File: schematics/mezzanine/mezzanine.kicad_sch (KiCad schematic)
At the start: 22 parts, among them J1 Bionic-P135, J10 Y0-7, J11 A0-7, J12 B0-7, J2 Bionic-P245, J3 Conn_01x24, J4 Conn_01x24, J5 P1P2, J6 P3P4, J7 P5, J8 5V0, J9 GND, U1 CPU, U2 11AA010-I/TT, U3 74AHCT157, U4 74AHCT157

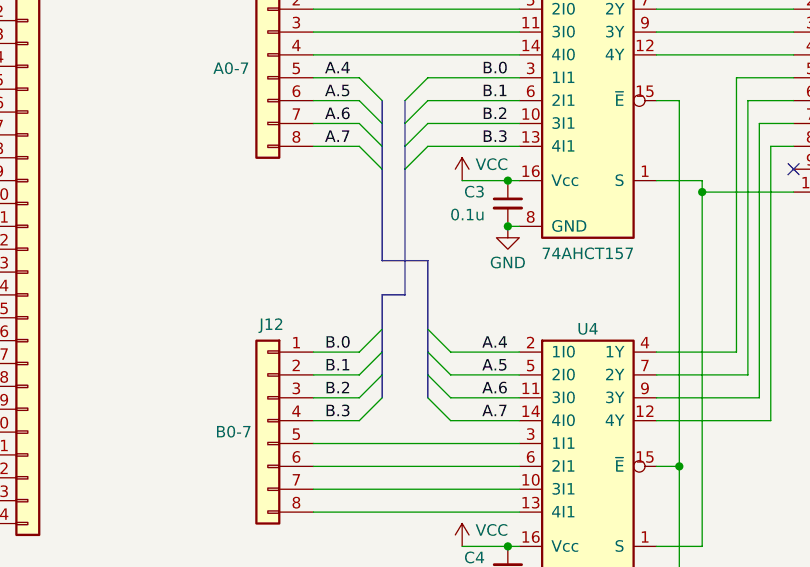
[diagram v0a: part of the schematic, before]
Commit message: [Mezzanine] Cleanup schematics
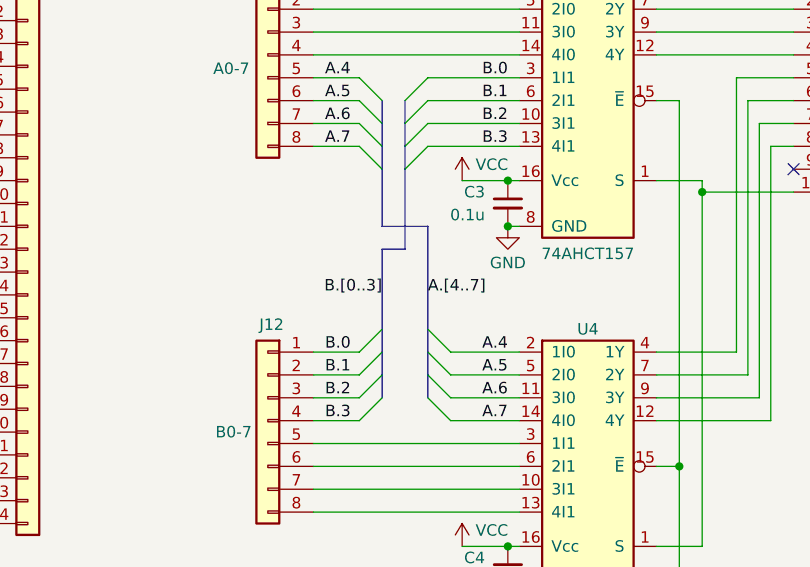
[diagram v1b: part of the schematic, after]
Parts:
- D1: footprint 0-LocalLibrary:LED_CSL1901UW1_ROM-M -> rhom:LED_CSL1901UW1_ROM-M; symbol 0-LocalLibrary:CSL1901UW1 -> rhom:CSL1901UW1
- J1: footprint 0-LocalLibrary:Bionic-P135_Vertical -> bionic:Bionic-P135_Vertical; symbol 0-LocalLibrary:Bionic-P135 -> bionic:Bionic-P135
- J2: footprint 0-LocalLibrary:Bionic-P245_Vertical -> bionic:Bionic-P245_Vertical; symbol 0-LocalLibrary:Bionic-P245 -> bionic:Bionic-P245
- U1: footprint 0-LocalLibrary:Aries_ZIF_socket_DIP-48-pin -> bionic:Aries_ZIF_socket_DIP-48-pin; symbol 0-LocalLibrary:CPU -> cpu:CPU
- U2: footprint 0-LocalLibrary:SOT-23_MC_MCH-M -> microchip:SOT-23_MC_MCH-M; symbol 0-LocalLibrary:11AA010-I_TT -> microchip:11AA010-I_TT
- U3, U4: footprint 0-LocalLibrary:PW16-M -> ti:PW16-M; symbol 0-LocalLibrary:74AHCT157 -> ti:74AHCT157

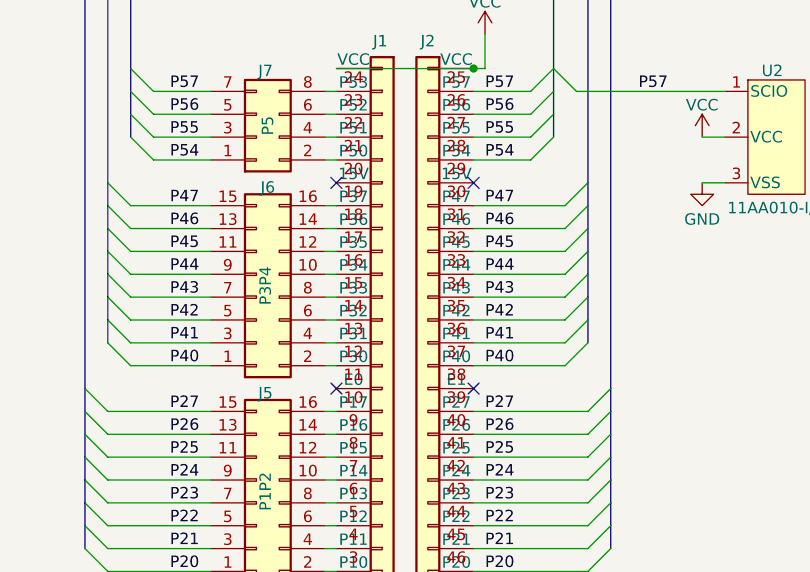
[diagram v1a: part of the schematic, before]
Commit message: [Mezzanine] Update schematics
Remove unused pins from bionic connector
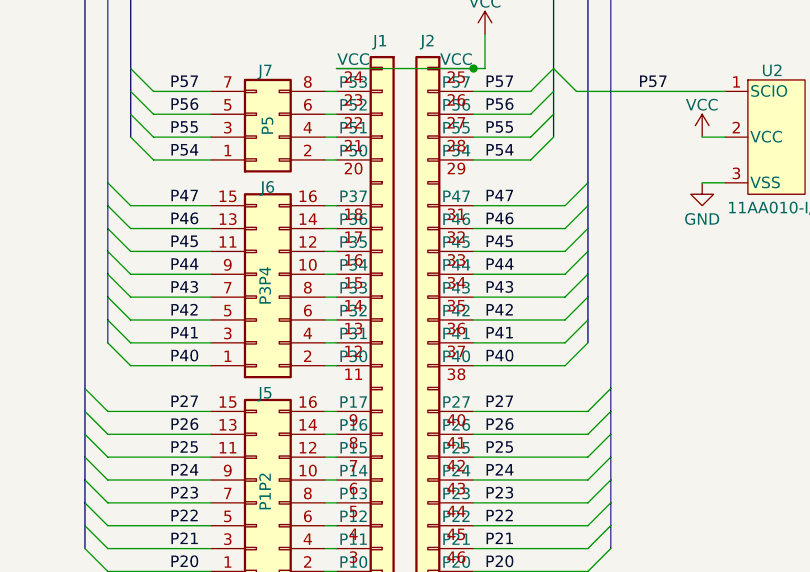
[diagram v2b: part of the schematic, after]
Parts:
- J1: footprint bionic:Bionic-P135_Vertical -> bionic:Bionic-P135_THT
- J2: footprint bionic:Bionic-P245_Vertical -> bionic:Bionic-P245_THT
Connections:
- no-connect marks 5 -> 1
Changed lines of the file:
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@@
 	(title_block
 		(title "BIonicMezzanine")
-		(date "2025-01-24")
-		(rev "1")
+		(date "2025-03-02")
+		(rev "2")
 	)
 	(junction
@@
 	)
 	(no_connect
-		(at 213.36 85.09)
-	)
-	(no_connect
-		(at 228.6 85.09)
-	)
-	(no_connect
 		(at 154.94 91.44)
 	)
-	(no_connect
-		(at 228.6 107.95)
-	)
-	(no_connect
-		(at 213.36 107.95)
-	)
 	(bus_entry
 		(at 109.22 116.84)
@@
 			)
 		)
-		(property "Footprint" "bionic:Bionic-P135_Vertical"
+		(property "Footprint" "bionic:Bionic-P135_THT"
 			(at 219.71 135.89 0)
 			(effects
@@
 		(pin "18"
 		)
-		(pin "10"
-		)
 		(pin "3"
 		)
@@
 		(pin "20"
 		)
-		(pin "19"
-		)
 		(pin "23"
 		)
@@
 			)
 		)
-		(property "Footprint" "bionic:Bionic-P245_Vertical"
+		(property "Footprint" "bionic:Bionic-P245_THT"
 			(at 228.6 135.89 0)
 			(effects
@@
 		(pin "42"
 		)
-		(pin "39"
-		)
 		(pin "28"
 		)
@@
 		(pin "41"
 		)
-		(pin "30"
-		)
 		(pin "45"
